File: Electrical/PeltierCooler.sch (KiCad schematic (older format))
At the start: 45 parts

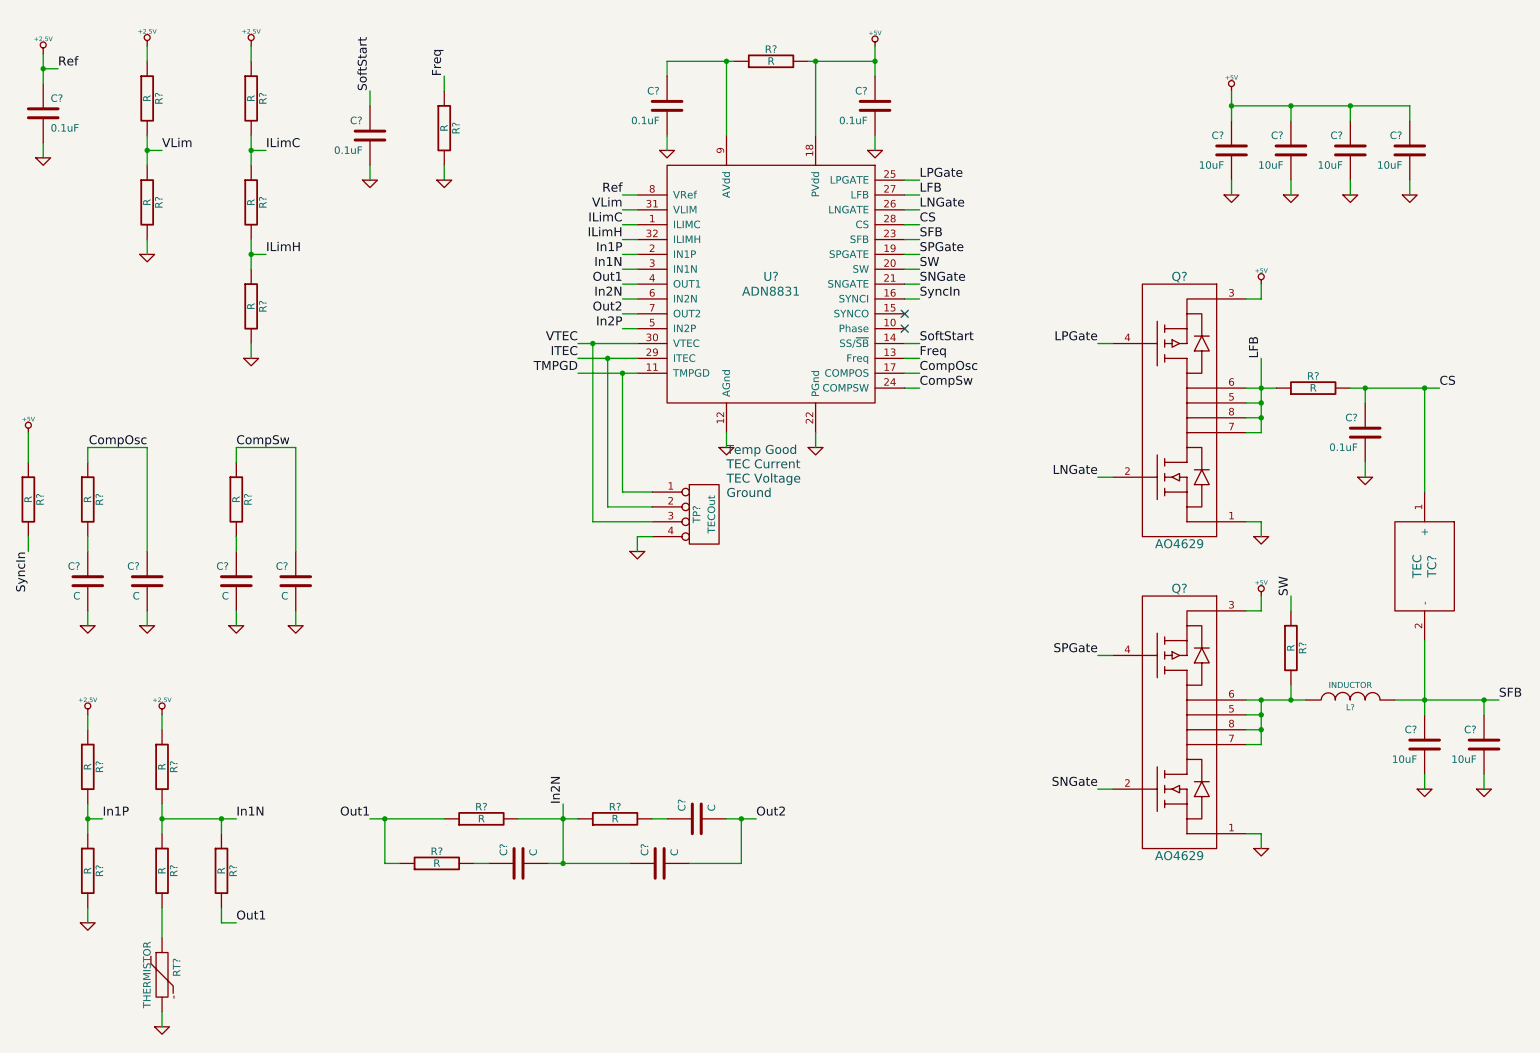
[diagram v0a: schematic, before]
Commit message: Added bias supply to schematic
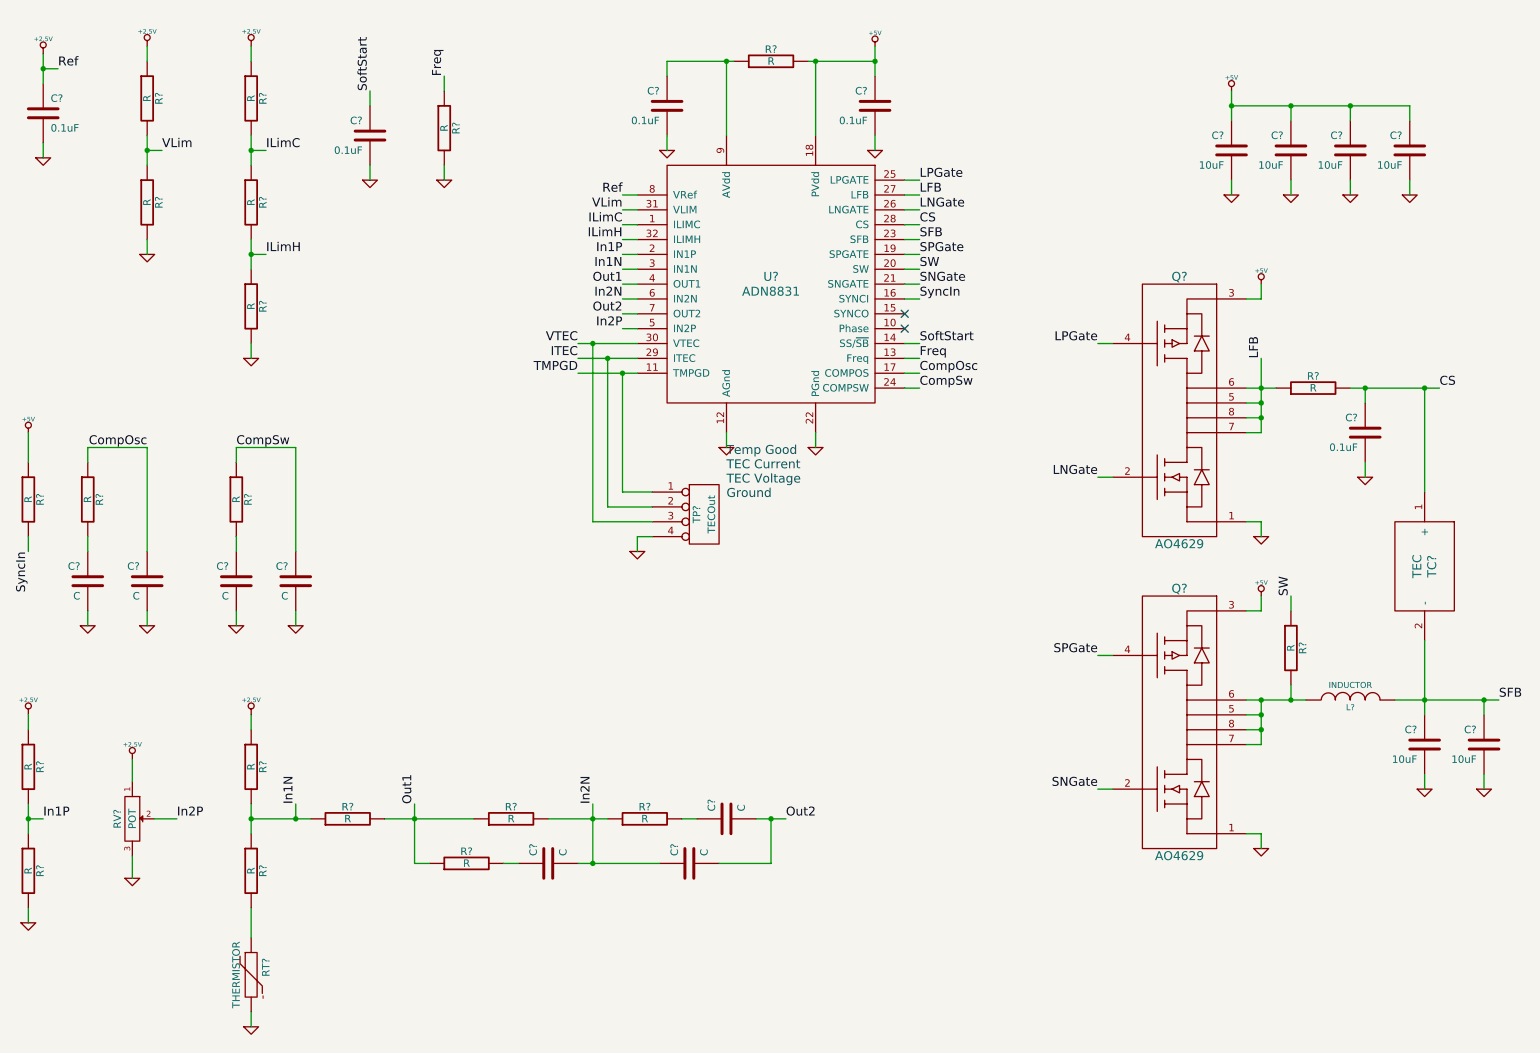
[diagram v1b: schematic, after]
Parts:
- added RV?: POT, symbol POT
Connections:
- net +2.5V: now also RV?.1
- net GND: now also RV?.3
- net In2P: now also RV?.2
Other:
- moved on the sheet: C?, R?, RT?

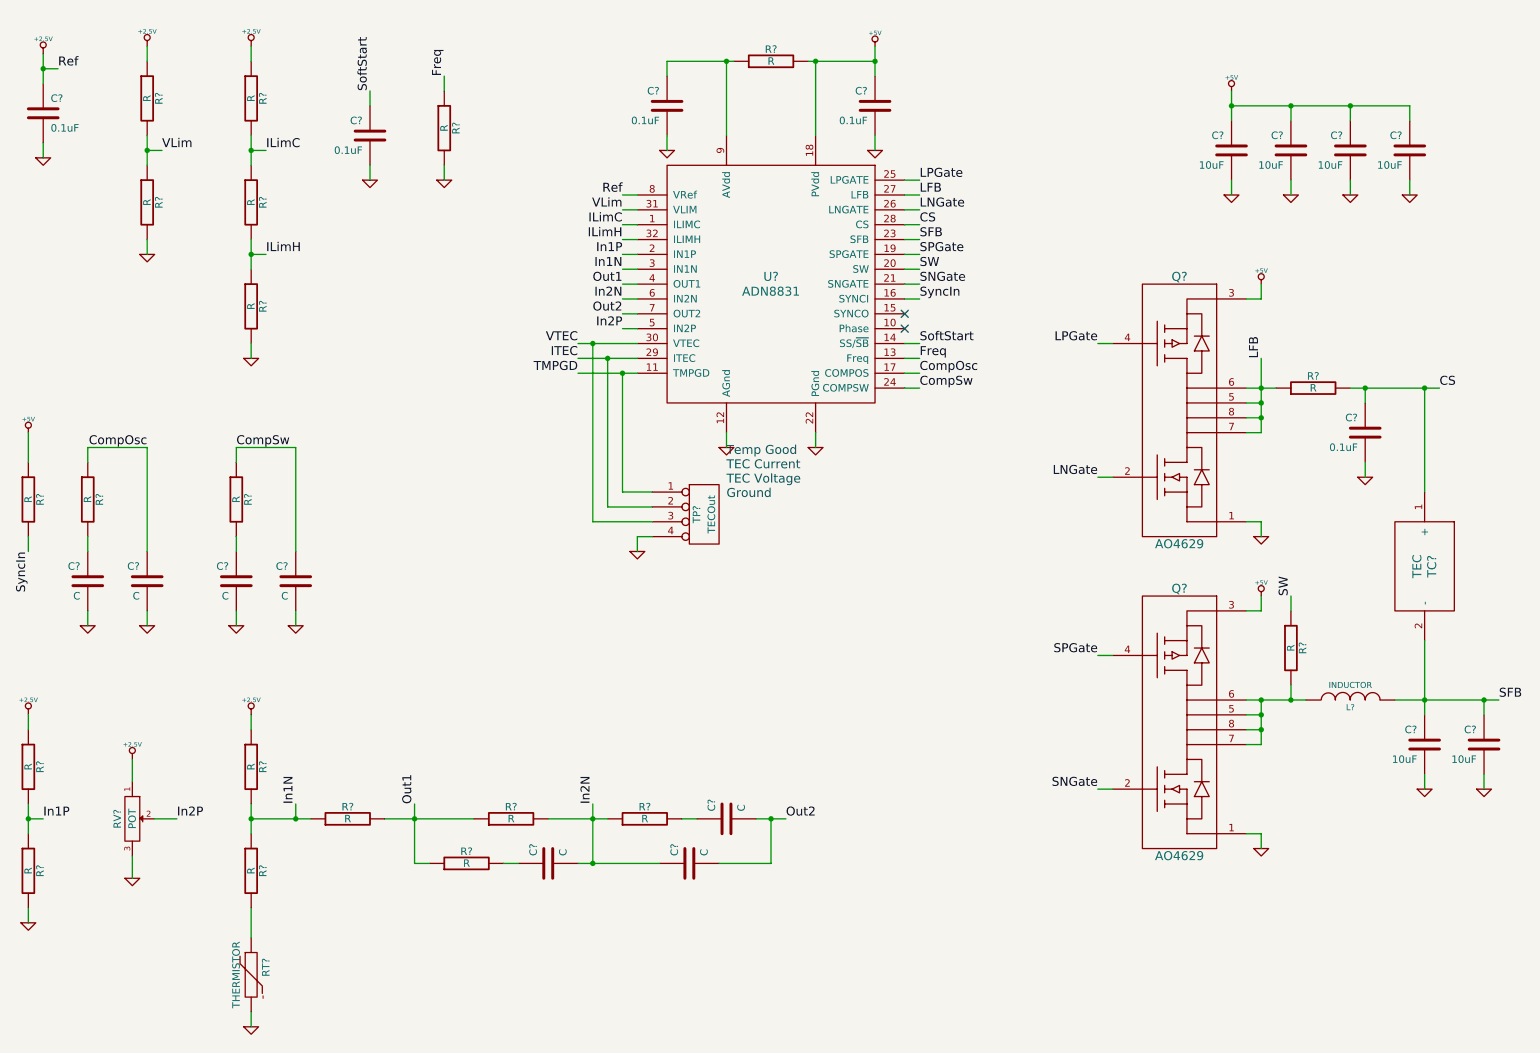
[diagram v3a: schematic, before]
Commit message: Added voltage references and test points
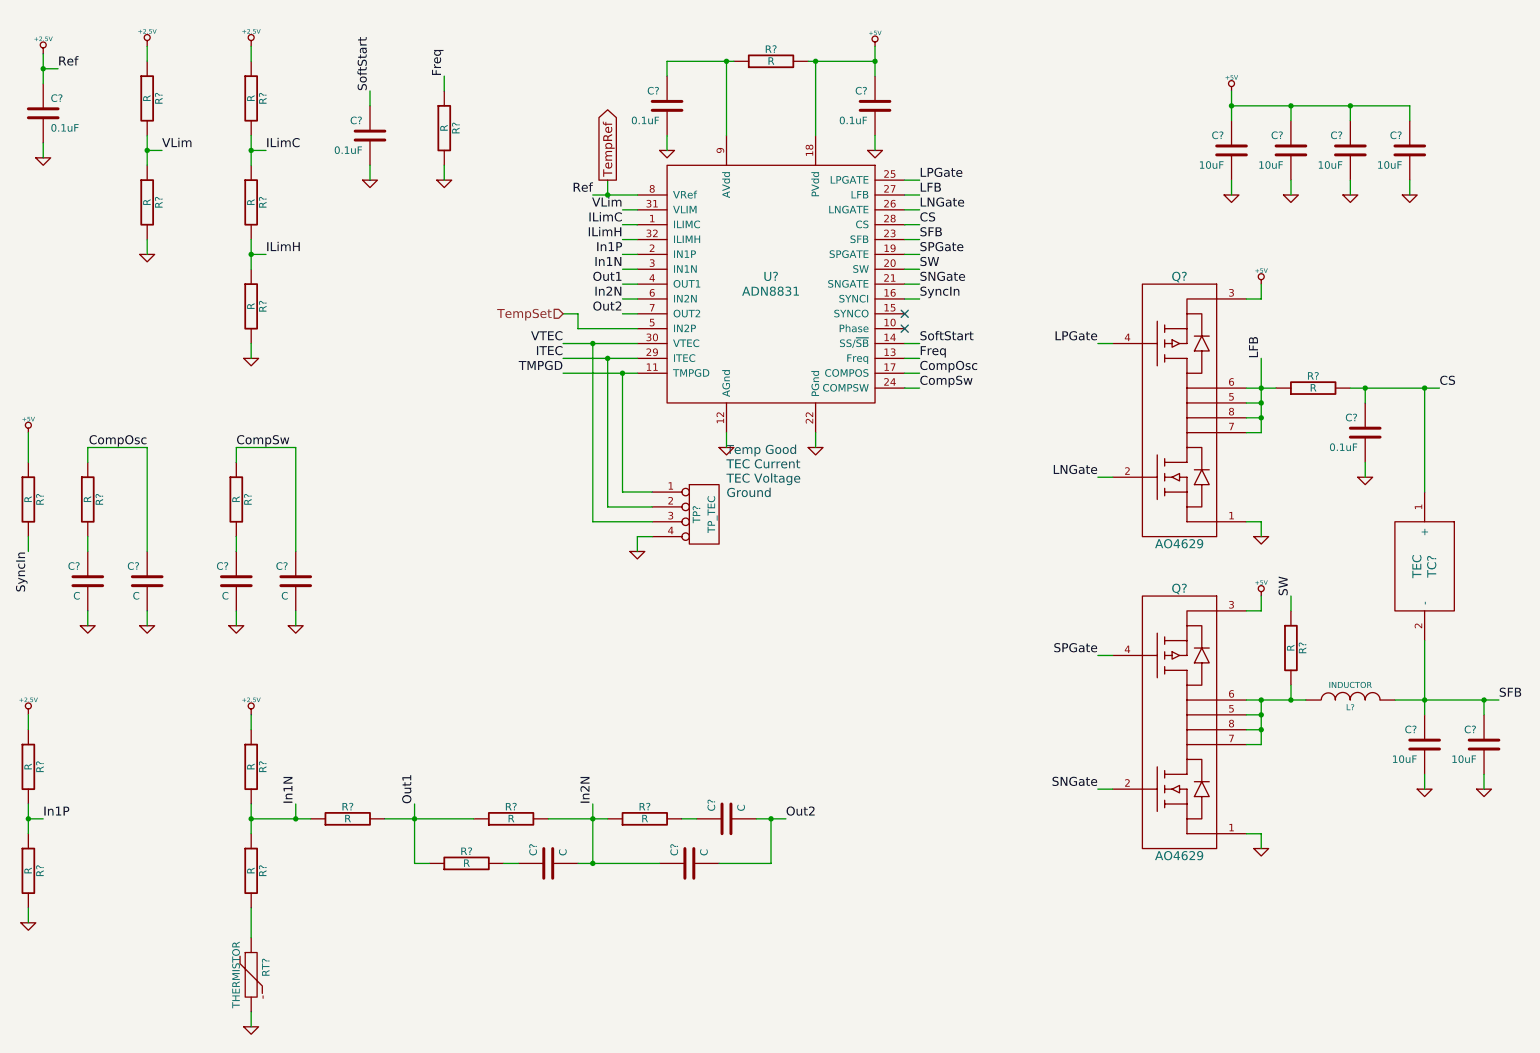
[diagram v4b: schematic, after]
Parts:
- removed RV?: POT, symbol POT
- TP?: value TECOut -> TP_TEC
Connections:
- net In2P renamed TempSet
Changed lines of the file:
@@
-EESchema Schematic File Version 2  date 4/17/2013 7:49:12 PM
+EESchema Schematic File Version 2  date 4/18/2013 6:48:03 PM
 LIBS:power
 LIBS:device
@@
 $Descr A4 11700 8267
 encoding utf-8
-Sheet 5 6
+Sheet 6 6
 Title "Cosmic Ray Detector"
-Date "17 apr 2013"
+Date "18 apr 2013"
 Rev "1A"
 Comp "Ethan Harstad"
@@
 Comment4 ""
 $EndDescr
-Wire Wire Line
-	1600 6400 1600 6250
-Wire Wire Line
-	1600 5600 1600 5750
+Connection ~ 4800 1800
+Wire Wire Line
+	4800 1700 4800 1800
 Wire Wire Line
 	3300 6000 3900 6000
@@
 Connection ~ 4800 2900
 Wire Wire Line
-	5000 2900 4600 2900
+	5000 2900 4500 2900
 Wire Wire Line
 	5100 4000 4700 4000
@@
 Wire Wire Line
 	6200 3500 6200 3400
-Wire Wire Line
-	4900 2700 5000 2700
 Wire Wire Line
 	4900 2600 5000 2600
@@
 	1000 850  1000 1050
 Wire Wire Line
-	4900 1800 5000 1800
+	4700 1800 5000 1800
 Wire Wire Line
 	4900 1900 5000 1900
@@
 	4800 3900 5100 3900
 Wire Wire Line
-	5000 2800 4600 2800
+	5000 2800 4500 2800
 Connection ~ 4700 2800
 Wire Wire Line
-	5000 3000 4600 3000
+	5000 3000 4500 3000
 Connection ~ 4900 3000
 Wire Wire Line
@@
 	3500 6300 3500 5900
 Wire Wire Line
-	1900 6000 1750 6000
-$Comp
-L GND #PWR?
-U 1 1 516B8B70
-P 1600 6400
-F 0 "#PWR?" H 1600 6400 30  0001 C CNN
-F 1 "GND" H 1600 6330 30  0001 C CNN
-	1    1600 6400
-	1    0    0    -1
-$EndComp
-Text Label 1900 6000 0    60   ~ 0
-In2P
-$Comp
-L +2.5V #PWR?
-U 1 1 516B8B53
-P 1600 5600
-F 0 "#PWR?" H 1600 5550 20  0001 C CNN
-F 1 "+2.5V" H 1600 5700 30  0000 C CNN
-	1    1600 5600
-	1    0    0    -1
-$EndComp
-$Comp
-L POT RV?
-U 1 1 516B8B3B
-P 1600 6000
-F 0 "RV?" H 1600 5900 50  0000 C CNN
-F 1 "POT" H 1600 6000 50  0000 C CNN
-	1    1600 6000
-	0    1    1    0
-$EndComp
+	4500 2600 4600 2600
+Wire Wire Line
+	4600 2600 4600 2700
+Wire Wire Line
+	4600 2700 5000 2700
+Text GLabel 4800 1700 1    60   Output ~ 0
+TempRef
+Text HLabel 4500 2600 0    60   Input ~ 0
+TempSet
 $Comp
 L +2.5V #PWR?
@@
 	1    0    0    -1
 $EndComp
-Text Label 4900 1800 2    60   ~ 0
+Text Label 4700 1800 2    60   ~ 0
 Ref
 Text Label 4900 1900 2    60   ~ 0
@@
 Text Label 4900 2600 2    60   ~ 0
 Out2
-Text Label 4900 2700 2    60   ~ 0
-In2P
 $Comp
 L GND #PWR?
@@
 P 5450 3950
 F 0 "TP?" V 5400 3950 50  0000 C CNN
-F 1 "TECOut" V 5500 3950 50  0000 C CNN
+F 1 "TP_TEC" V 5500 3950 50  0000 C CNN
 	1    5450 3950
 	1    0    0    -1
@@
 	1    0    0    -1
 $EndComp
-Text Label 4600 2800 2    60   ~ 0
+Text Label 4500 2800 2    60   ~ 0
 VTEC
-Text Label 4600 2900 2    60   ~ 0
+Text Label 4500 2900 2    60   ~ 0
 ITEC
-Text Label 4600 3000 2    60   ~ 0
+Text Label 4500 3000 2    60   ~ 0
 TMPGD
 Text Notes 5600 3850 0    60   ~ 0

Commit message: Adding schematic annotations to explain functions
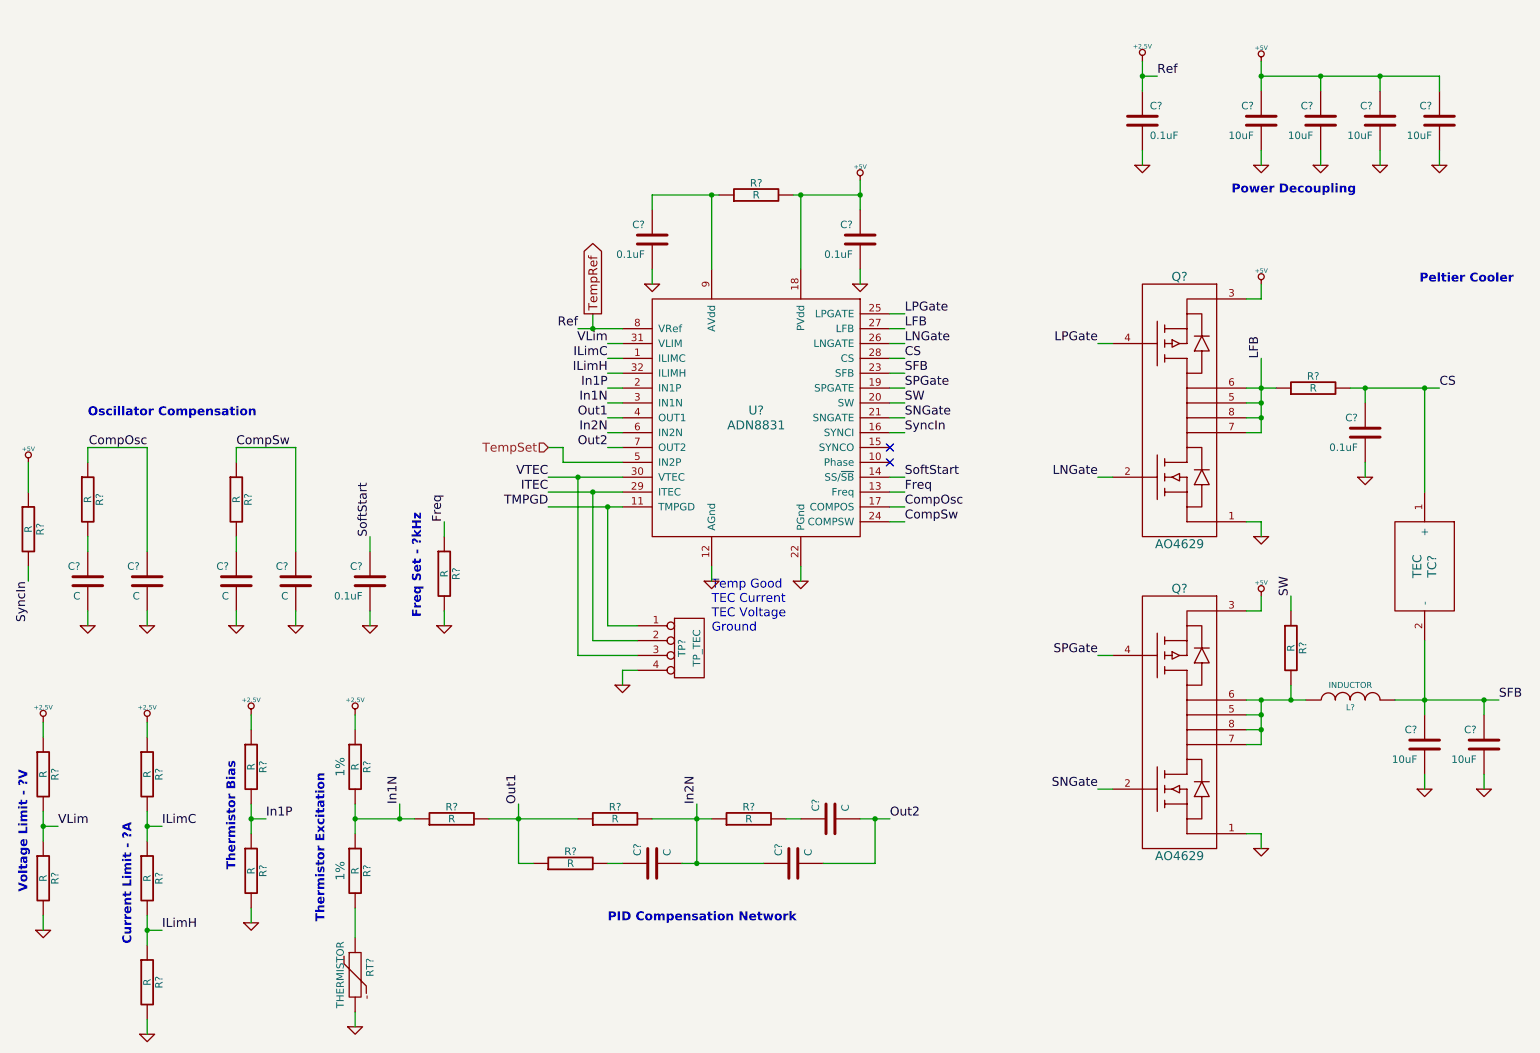
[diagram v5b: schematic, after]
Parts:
- removed R?: R, symbol R
- added R?: R, symbol R
- R?: Tolerance (none) -> 1%
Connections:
- net +2.5V: now also R?.1
- net In1N: now also R?.2
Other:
- note added: "Current Limit - ?A"
- note added: "Freq Set - ?kHz"
- note added: "Oscillator Compensation"
- note added: "PID Compensation Network"
- note added: "Peltier Cooler"
- note added: "Power Decoupling"
- note added: "Thermistor Bias"
- note added: "Thermistor Excitation"
- note added: "Voltage Limit - ?V"
- moved on the sheet: C?, R?, RT?, TP?, U?
